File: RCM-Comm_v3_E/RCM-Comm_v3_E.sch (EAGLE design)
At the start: 37 parts, among them J1 BLACKFIN_HEADER, J3 USB-MICROB, U1 LANTRONIX_XPICO

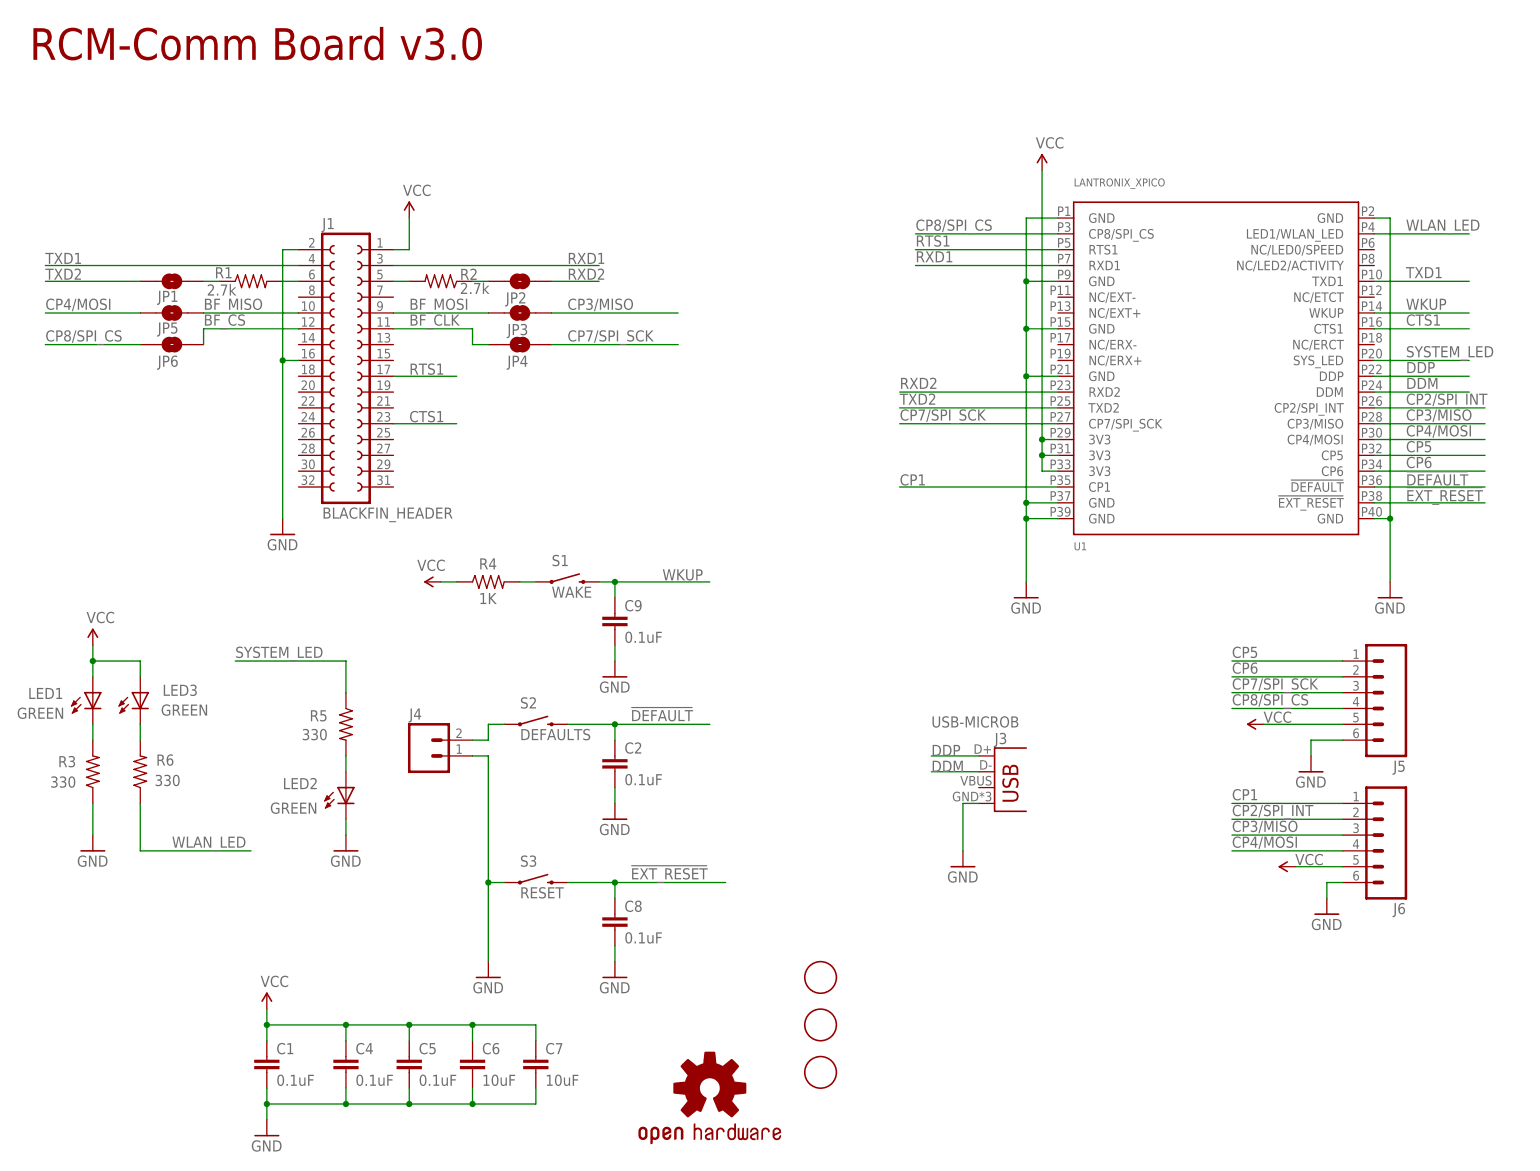
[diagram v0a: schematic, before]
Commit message: Got Ethernet version of RCM-Comm_v3 board pretty much done. Out for Tim's review.
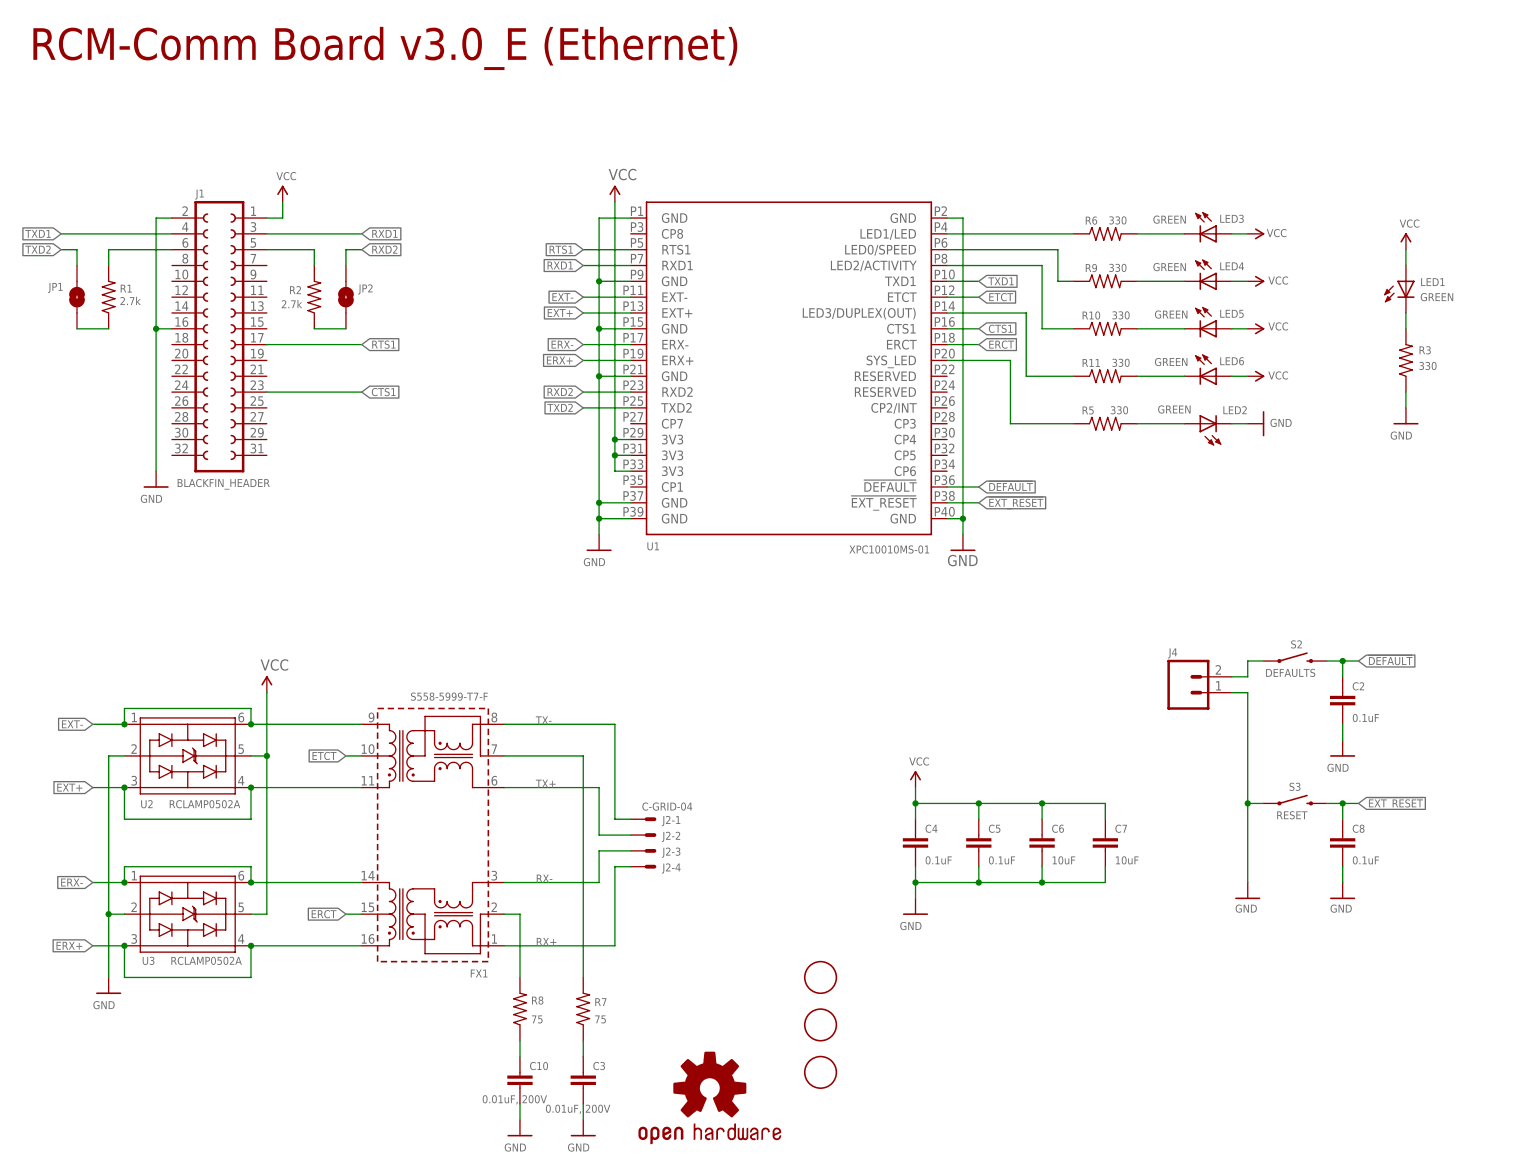
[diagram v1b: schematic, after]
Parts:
- removed C1, C9: 0.1uF, SparkFun-Capacitors:0.1UF-25V(+80/-20%)(0603)
- removed J3: USB-MICROB, SparkFun-Connectors:USB-MICROB
- removed J5, J6: (no value), SparkFun-Connectors:M06LOCK
- removed JP3, JP4, JP5, JP6: JUMPER-PAD-2-NOROUND, SparkFun-Passives:JUMPER-PAD-2-NOROUND
- removed R4: 1K, rcl:R-US_R0603
- removed S1: WAKE, SparkFun-Electromechanical:SWITCH-MOMENTARY-2SMD
- added C10, C3: 0.01uF, 200V, spark_fun:CAP0603-CAP
- added FX1: S558-5999-T7-F, halo-electronics:TG110-E050N5
- added J2-: C-GRID-04, MolexConnector:C-GRID-04
- added LED4, LED5, LED6: GREEN, spark_fun:LED0603
- added R10, R11, R9: 330, spark_fun:RESISTOR0603-RES
- added R7, R8: 75, rcl:R-US_R0603
- added U2, U3: RCLAMP0502A, SemtechRCLAMP:RCLAMP0502A
- U1: value LANTRONIX_XPICO -> XPC10010MS-01; device xPico:LANTRONIX_XPICO -> xPicoEthernet:LANTRONIX_XPICO
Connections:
- net N$24 renamed TXD2_J1
- net N$26 renamed RXD2_J1
- removed net BF_CLK: J1.SPI_SCK, JP4.1
- removed net BF_CS: J1.SPI_SEL, JP6.2
- removed net BF_MISO: J1.SPI_MISO, JP5.2
- removed net BF_MOSI: J1.SPI_MOSI, JP3.1
- removed net CP1: J6.1, U1.CP1
- removed net CP2/SPI_INT: J6.2, U1.CP2/SPI_INT
- removed net CP3/MISO: J6.3, JP3.2, U1.CP3/MISO
- removed net CP4/MOSI: J6.4, JP5.1, U1.CP4/MOSI
- removed net CP5: J5.1, U1.CP5
- removed net CP6: J5.2, U1.CP6
- removed net CP7/SPI_SCK: J5.3, JP4.2, U1.CP7/SPI_SCK
- removed net CP8/SPI_CS: J5.4, JP6.1, U1.CP8/SPI_CS
- removed net DDM: J3.D-, U1.DDM
- removed net DDP: J3.D+, U1.DDP
- removed net N$5: R4.2, S1.1
- removed net WKUP: C9.1, S1.2, U1.WKUP
- removed net WLAN_LED: R6.1, U1.LED1/WLAN_LED
- new net ERCT: FX1.15, U1.ERCT
- new net ERX+: FX1.16, U1.ERX+, U3.P$3, U3.P$4
- new net ERX-: FX1.14, U1.ERX-, U3.P$1, U3.P$6
- new net ETCT: FX1.10, U1.ETCT
- new net EXT+: FX1.11, U1.EXT+, U2.P$3, U2.P$4
- new net EXT-: FX1.9, U1.EXT-, U2.P$1, U2.P$6
- new net LED0_SPEED: R9.1, U1.LED0/SPEED
- new net LED1_LINK: R6.1, U1.LED1/LED
- new net LED2_ACTIVITY: R10.1, U1.LED2/ACTIVITY
- new net LED3_DUPLEX: R11.1, U1.LED3/DUPLEX(OUT)
- new net N$10: C3.1, R7.1
- new net N$11: FX1.7, R7.2
- new net N$14: LED6.C, R11.2
- new net N$15: LED5.C, R10.2
- new net N$16: LED4.C, R9.2
- new net N$7: FX1.2, R8.2
- new net N$9: C10.1, R8.1
- new net RX+: FX1.1, J2-4.S
- new net RX-: FX1.3, J2-3.S
- new net TX+: FX1.6, J2-2.S
- new net TX-: FX1.8, J2-1.S
- net GND: now also C10.2, C3.2, U2.P$2, U3.P$2; no longer C1.2, C9.2, J3.GND, J5.6, J6.6
- net VCC: now also LED4.A, LED5.A, LED6.A, U2.P$5, U3.P$5; no longer C1.1, J5.5, J6.5, R4.1
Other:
- note added: "ACTIVITY"
- note added: "Copyright 2019 Engineering^3 LLC"
- note added: "Copyright 2019 Engineering^3 LLC Copyright and related rights are licensed under the Solderpad Hardware License, Version 0.51 (the “License”); you may not use this file except in compliance with the License. You may obtain a copy of the License at http://solderpad.org/licenses/SHL-0.51. Unless required by applicable law or agreed to in writing, software, hardware and materials distributed under t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"
- note added: "DUPLEX"
- note added: "LINK"
- note added: "POWER"
- note added: "RCM-Comm Board v3.0_E (Ethernet)"
- note added: "SPEED"
- note added: "STATUS"
- note added: "Short J4 to enable resetting to defaults with DEFAULT button"
- note removed: "Copyright 2016 Engineering^3 LLC"
- note removed: "Copyright 2016 Engineering^3 LLC Copyright and related rights are licensed under the Solderpad Hardware License, Version 0.51 (the “License”); you may not use this file except in compliance with the License. You may obtain a copy of the License at http://solderpad.org/licenses/SHL-0.51. Unless required by applicable law or agreed to in writing, software, hardware and materials distributed under t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"
- note removed: "Do Not Place"
- note removed: "RCM-Comm Board v3.0"
- moved on the sheet: C2, C4, C5, C6, C7, C8, J1, J4, JP1, JP2, LED1, LED2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
